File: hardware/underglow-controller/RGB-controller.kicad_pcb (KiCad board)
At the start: 4 copper layers, 86 x 97.7 mm, 139 parts, among them J2 U.FL-R-SMT-1(10), J3 DM3AT-SF-PEJM5, J4 DTM1312PA12PBR008, J5 Conn_01x10, J6 CONSOLE, J7 U.FL-R-SMT-1(10), J8 JTAG, Q2 STS8DNF3LL, Q3 STS8DNF3LL, Q4 STS8DNF3LL, SW2 SW_Push, SW3 SW_Push, SW4 SW_Push, U10 DRV8844PWP, U11 RP2040, U3 SN65HVD230, U4 ESP32-S3R2, U5 W25Q128JVS, U6 WS2815B, U7 W25Q128JVS, U8 ADP2303ARDZ-3.3, U9 COM-13909, Y2 40MHZ, Y3 32.7k, Y4 40MHZ

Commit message: Fill out BOM for mouser
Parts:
- removed C2: 1uF, Capacitor_SMD:C_0402_1005Metric
- removed R2: 442k, Resistor_SMD:R_0402_1005Metric
- AE2: value Antenna_Shield -> PCB_ANT
- AE3: value Antenna_Shield -> PCB_ANT_RFM69
- D5: footprint Diode_SMD:D_SOD-123 -> Diode_SMD:D_SOD-123F
- R23: value 100k -> 10k
- R39: footprint Resistor_SMD:R_0603_1608Metric -> Resistor_SMD:R_0402_1005Metric
- moved D5 0.28 mm to (89.6, 55.2)
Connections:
- U4 pad 36: /SPICLK_N -> unconnected-(U4-Pad36)
- U4 pad 37: /SPICLK_P -> unconnected-(U4-Pad37)
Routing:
- net /SPICLK_P: track 7.04 -> 0.00 mm
- net GND: track 132.8 -> 130.2 mm, vias 79 -> 78
- net Net-(C42-Pad1): track 1.58 -> 2.18 mm

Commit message: gerbertiem
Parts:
- moved C14 0.46 mm to (49.7, 111.3)
- moved C16 0.46 mm to (48.7, 111.3)
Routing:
- net /GPIO_GPO4: track 40.6 -> 38.2 mm
- net /GPIO_GPO1: track 45.3 -> 43.6 mm
- net +3V3: track 535.4 -> 536.3 mm
- net /FSPICLK: track 217.0 -> 217.8 mm
- net /FSPID: track 225.5 -> 226.3 mm
- net /FSPIQ: track 225.8 -> 226.4 mm

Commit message: bom bom bom bom
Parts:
- moved C40 0.11 mm to (46.6, 72.1)
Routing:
- net /SPICS1: track 36.9 -> 0.00 mm, vias 1 -> 0
- net +3V3: track 536.3 -> 528.7 mm, vias 24 -> 32
- net /GPIO_GPO5: track 38.3 -> 35.0 mm
- net GND: track 130.2 -> 129.9 mm, vias 78 -> 81
- net /SW: vias 2 -> 4

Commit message: Submit for fab. tagme
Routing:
- net +3V3: track 528.7 -> 534.2 mm
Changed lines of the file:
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@@
   (segment (start 73.98 76.77) (end 73.98 74.79) (width 1) (layer "B.Cu") (net 13))
   (segment (start 77.9 75.86) (end 79.07 75.86) (width 1) (layer "B.Cu") (net 13))
-  (segment (start 103.61 117.14) (end 103.61 119.22) (width 1) (layer "B.Cu") (net 13))
+  (segment (start 87.74 116.3) (end 89.02 117.58) (width 1) (layer "B.Cu") (net 13))
   (segment (start 39.64 103.97) (end 41.28 105.61) (width 0.5) (layer "B.Cu") (net 13))
   (segment (start 76.69 75.86) (end 77.9 75.86) (width 1) (layer "B.Cu") (net 13))
   (segment (start 56.09 78.1) (end 54.23 79.96) (width 1) (layer "B.Cu") (net 13))
   (segment (start 46.12 72.97) (end 46.12 67.59666) (width 1) (layer "B.Cu") (net 13))
+  (segment (start 89.56 117.04) (end 89.02 117.58) (width 1) (layer "B.Cu") (net 13))
   (segment (start 38.44 125.205) (end 38.44 129.06) (width 0.5) (layer "B.Cu") (net 13))
   (segment (start 55.19 124.81) (end 55.4 124.6) (width 0.5) (layer "B.Cu") (net 13))
   (segment (start 71.18 71.99) (end 71.18 62.33) (width 1) (layer "B.Cu") (net 13))
+  (segment (start 83.23 116.3) (end 87.74 116.3) (width 1) (layer "B.Cu") (net 13))
   (segment (start 55.86 115.92) (end 55.4 116.38) (width 0.5) (layer "B.Cu") (net 13))
-  (segment (start 103.56 117.04) (end 92.35 117.04) (width 1) (layer "B.Cu") (net 13))
   (segment (start 35.06 72.77) (end 35.05 72.78) (width 0.5) (layer "B.Cu") (net 13))
   (segment (start 54.23 79.96) (end 49.7 79.96) (width 1) (layer "B.Cu") (net 13))
@@
   (segment (start 36.81 100.6305) (end 36.81 103.95) (width 0.5) (layer "B.Cu") (net 13))
   (segment (start 55.86 115.92) (end 55.528415 115.588415) (width 1) (layer "B.Cu") (net 13))
-  (segment (start 90.457499 118.932501) (end 90.377499 118.932501) (width 1) (layer "B.Cu") (net 13))
-  (segment (start 103.61 119.22) (end 101.47 121.36) (width 1) (layer "B.Cu") (net 13))
   (segment (start 46.1 67.57666) (end 46.1 65.4) (width 1) (layer "B.Cu") (net 13))
   (segment (start 56.24 116.3) (end 55.86 115.92) (width 1) (layer "B.Cu") (net 13))
@@
   (segment (start 91.14 119.695003) (end 90.377499 118.932501) (width 1) (layer "B.Cu") (net 13))
   (segment (start 41.27 110.27) (end 41.28 110.28) (width 0.5) (layer "B.Cu") (net 13))
+  (segment (start 97.64 119.22) (end 99.78 121.36) (width 1) (layer "B.Cu") (net 13))
   (segment (start 46.1 65.4) (end 42.18 61.48) (width 1) (layer "B.Cu") (net 13))
   (segment (start 53.43 124.81) (end 52.07 123.45) (width 0.5) (layer "B.Cu") (net 13))
@@
   (segment (start 89.024998 117.58) (end 90.377499 118.932501) (width 1) (layer "B.Cu") (net 13))
   (segment (start 35.06 65.27) (end 38.85 61.48) (width 0.5) (layer "B.Cu") (net 13))
-  (segment (start 101.47 121.36) (end 99.78 121.36) (width 1) (layer "B.Cu") (net 13))
   (segment (start 35.51 103.97) (end 36.79 103.97) (width 0.5) (layer "B.Cu") (net 13))
   (segment (start 104.45 79.3) (end 104.43 79.32) (width 1) (layer "B.Cu") (net 13))
@@
   (segment (start 55.528415 115.518415) (end 55.528415 115.588415) (width 0.5) (layer "B.Cu") (net 13))
   (segment (start 35.05 72.78) (end 35.05 75.16) (width 0.5) (layer "B.Cu") (net 13))
-  (segment (start 92.35 117.04) (end 90.457499 118.932501) (width 1) (layer "B.Cu") (net 13))
   (segment (start 43.16 120.485) (end 38.44 125.205) (width 0.5) (layer "B.Cu") (net 13))
+  (segment (start 103.56 117.04) (end 89.56 117.04) (width 1) (layer "B.Cu") (net 13))
   (segment (start 35.05 75.16) (end 37.318816 77.428816) (width 0.5) (layer "B.Cu") (net 13))
   (segment (start 49.7 79.96) (end 46.119992 76.379992) (width 1) (layer "B.Cu") (net 13))
@@
   (segment (start 64.565 55.715) (end 52.39 55.715) (width 1) (layer "B.Cu") (net 13))
   (segment (start 54.893589 114.883589) (end 55.528415 115.518415) (width 0.5) (layer "B.Cu") (net 13))
+  (segment (start 97.64 117.09) (end 97.64 119.22) (width 1) (layer "B.Cu") (net 13))
   (segment (start 52.786828 112.78) (end 49.18 112.78) (width 0.5) (layer "B.Cu") (net 13))
   (segment (start 54.890417 114.883589) (end 52.786828 112.78) (width 0.5) (layer "B.Cu") (net 13))

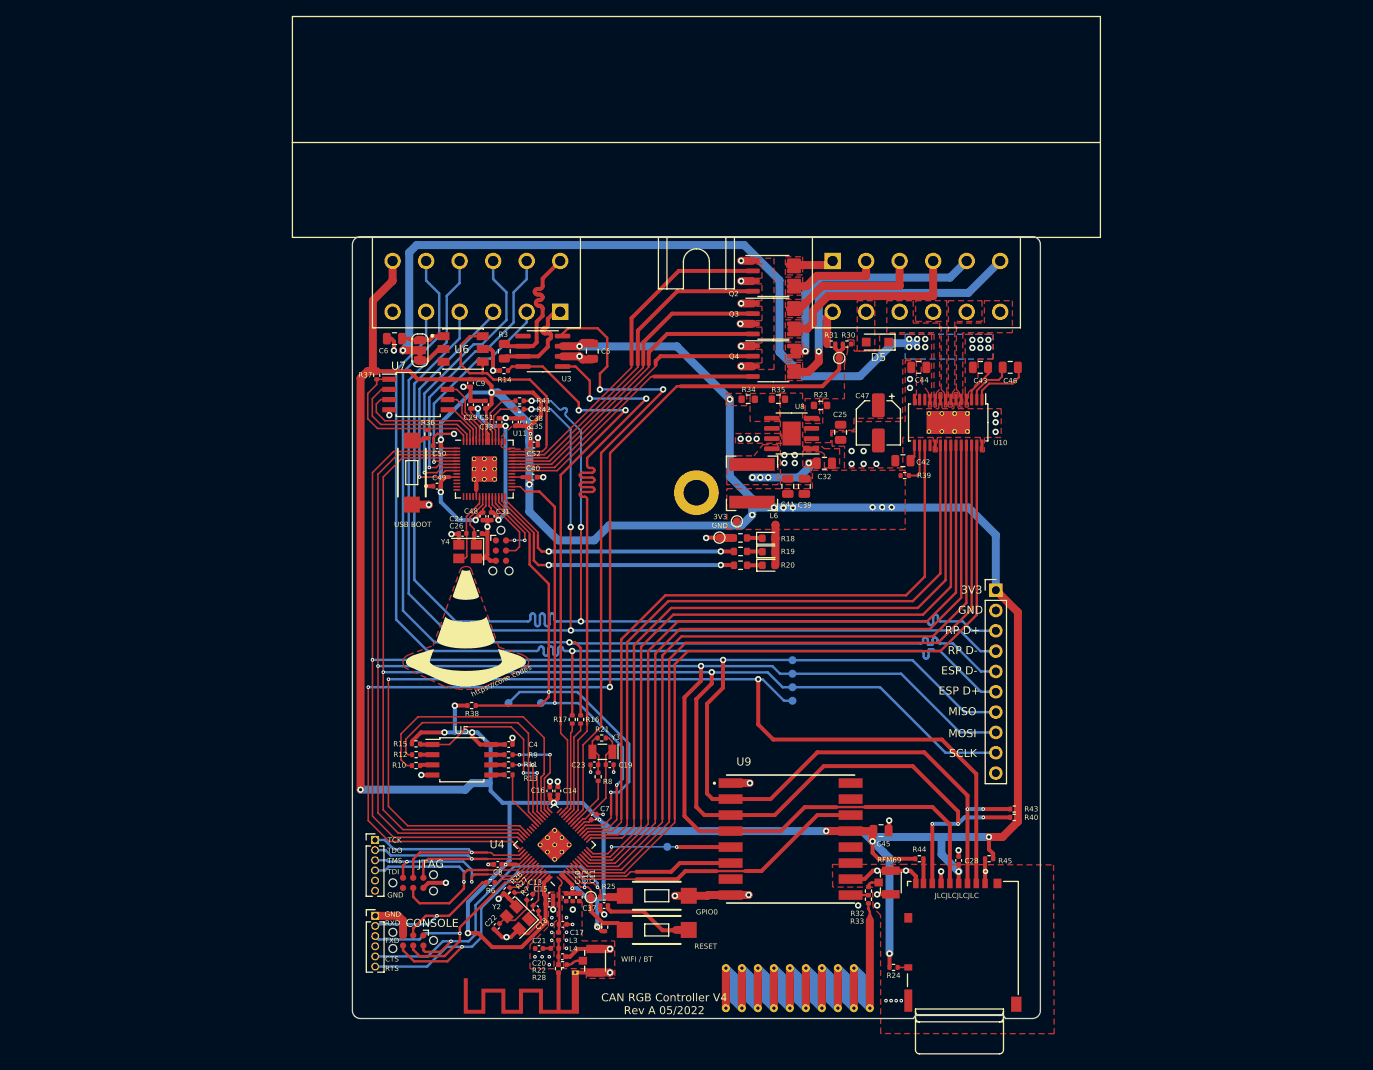
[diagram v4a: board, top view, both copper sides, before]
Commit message: hardware updates: fix SPI bus on pico and flatten radio module
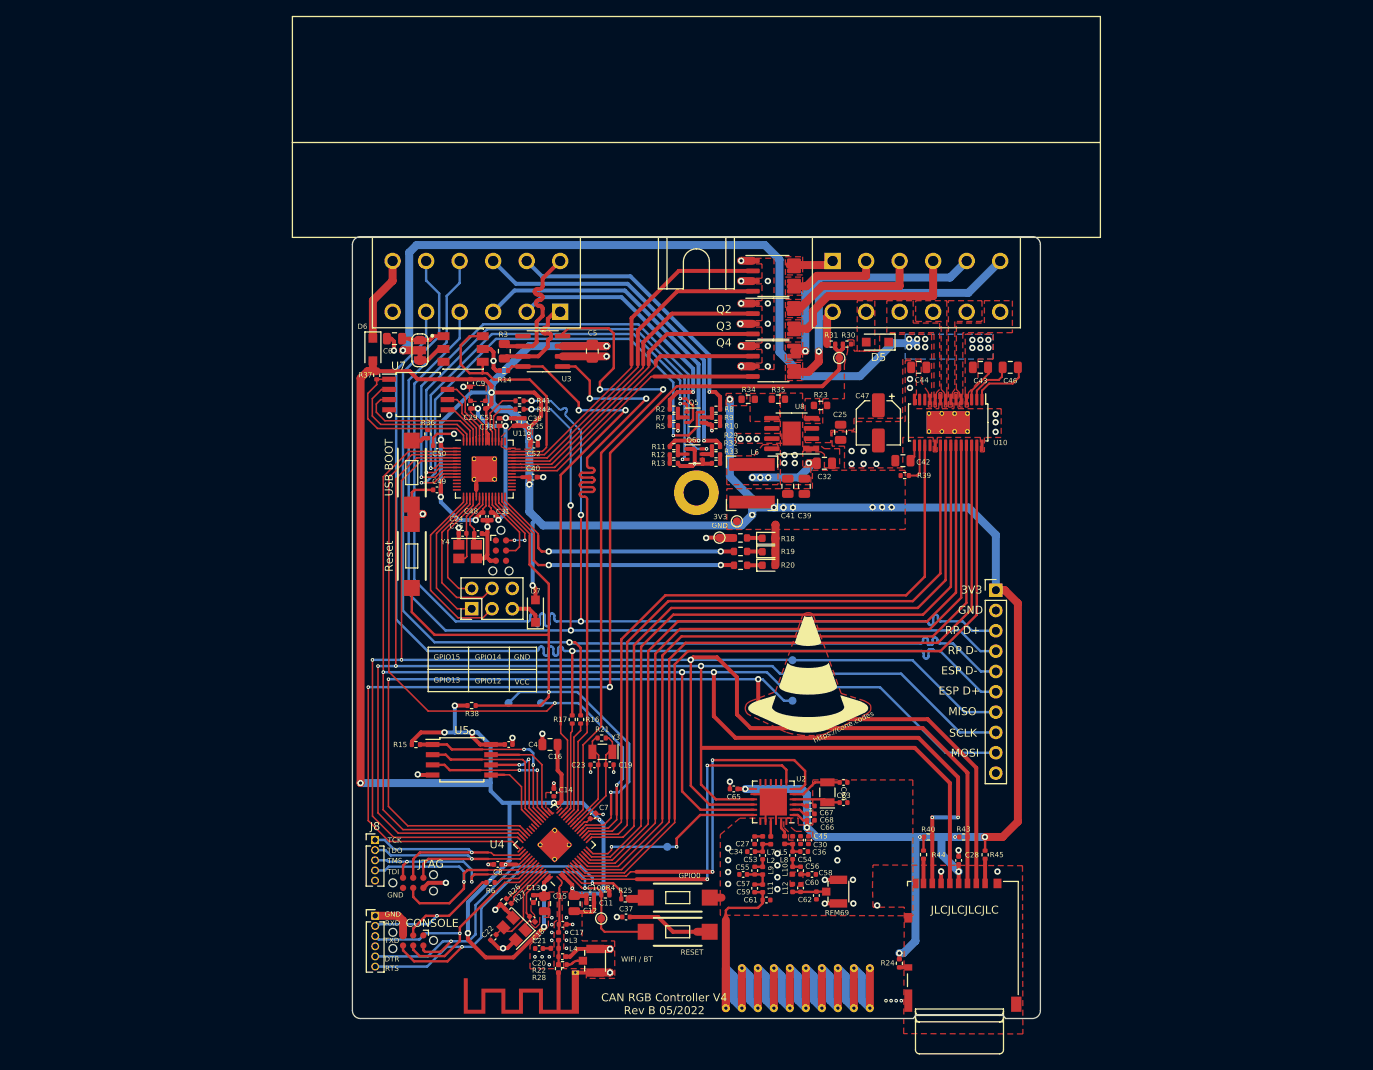
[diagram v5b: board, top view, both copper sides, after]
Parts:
- removed U9: COM-13909, ConeCodes:XCVR_RFM69HW
- added C27: C_Small, Capacitor_SMD:C_0402_1005Metric, F.Cu at (74.3, 117.5)
- added C30: C_Small, Capacitor_SMD:C_0402_1005Metric, F.Cu at (80.0, 117.4)
- added C34: C_Small, Capacitor_SMD:C_0402_1005Metric, F.Cu at (73.8, 118.9)
- added C36: C_Small, Capacitor_SMD:C_0402_1005Metric, F.Cu at (80.5, 118.9)
- added C53: C_Small, Capacitor_SMD:C_0402_1005Metric, F.Cu at (75.3, 119.3)
- added C54: C_Small, Capacitor_SMD:C_0402_1005Metric, F.Cu at (79.0, 119.3)
- added C55: C_Small, Capacitor_SMD:C_0402_1005Metric, F.Cu at (74.3, 121.2)
- added C56: C_Small, Capacitor_SMD:C_0402_1005Metric, F.Cu at (80.0, 121.2)
- added C57: C_Small, Capacitor_SMD:C_0402_1005Metric, F.Cu at (72.8, 121.7)
- added C58: C_Small, Capacitor_SMD:C_0402_1005Metric, F.Cu at (81.5, 121.7)
- added C59: C_Small, Capacitor_SMD:C_0402_1005Metric, F.Cu at (74.3, 123.5)
- added C60: C_Small, Capacitor_SMD:C_0402_1005Metric, F.Cu at (80.0, 123.4)
- added C61: C_Small, Capacitor_SMD:C_0402_1005Metric, F.Cu at (75.8, 124.9)
- added C62: C_Small, Capacitor_SMD:C_0402_1005Metric, F.Cu at (82.0, 124.3)
- added C63: 10pF, Capacitor_SMD:C_0402_1005Metric, F.Cu at (85.4, 112.7)
- added C64: 10pF, Capacitor_SMD:C_0402_1005Metric, F.Cu at (85.4, 110.2)
- added C65: 0.1uF, Capacitor_SMD:C_0402_1005Metric, F.Cu at (71.7, 111.0)
- added C66: 0.1uF, Capacitor_SMD:C_0402_1005Metric, F.Cu at (81.3, 115.0)
- added C67: 0.1uF, Capacitor_SMD:C_0402_1005Metric, F.Cu at (81.3, 113.2)
- added C68: 0.1uF, Capacitor_SMD:C_0402_1005Metric, F.Cu at (81.3, 114.2)
- added D6: D_Small, Diode_SMD:D_SOD-123F, F.Cu at (26.6, 56.1)
- added D7: D_Small, Diode_SMD:D_SOD-123F, F.Cu at (46.9, 88.8)
- added J9: Conn_01x10, Connector_PinHeader_2.54mm:PinHeader_2x03_P2.54mm_Vertical, F.Cu at (38.9, 88.5)
- added L10: L_Small, Inductor_SMD:L_0402_1005Metric, F.Cu at (79.0, 121.2)
- added L11: L_Small, Inductor_SMD:L_0402_1005Metric, F.Cu at (75.3, 123.5)
- added L12: L_Small, Inductor_SMD:L_0402_1005Metric, F.Cu at (79.0, 123.4)
- added L2: L_Small, Inductor_SMD:L_0402_1005Metric, F.Cu at (76.3, 117.5)
- added L5: L_Small, Inductor_SMD:L_0402_1005Metric, F.Cu at (78.0, 117.4)
- added L7: L_Small, Inductor_SMD:L_0402_1005Metric, F.Cu at (75.3, 117.5)
- added L8: L_Small, Inductor_SMD:L_0402_1005Metric, F.Cu at (79.0, 117.4)
- added L9: L_Small, Inductor_SMD:L_0402_1005Metric, F.Cu at (75.3, 121.2)
- added Q5: MBT3904DW1T1G, Package_TO_SOT_SMD:SOT-363_SC-70-6, F.Cu at (66.8, 64.6)
- added Q6: MBT3904DW1T1G, Package_TO_SOT_SMD:SOT-363_SC-70-6, F.Cu at (66.8, 69.2)
- added R2: 10k, Resistor_SMD:R_0402_1005Metric, F.Cu at (64.2, 63.6)
- added R29: 10k, Resistor_SMD:R_0402_1005Metric, F.Cu at (69.5, 68.2)
- added R5: 1k, Resistor_SMD:R_0402_1005Metric, F.Cu at (64.2, 64.6)
- added SW5: SW_Push, ConeCodes:SW_RS-032G05A3-SMRT, F.Cu at (31.4, 81.9)
- added U2: SX1231HIMLTRT, Package_DFN_QFN:QFN-24-1EP_5x5mm_P0.65mm_EP3.4x3.4mm, F.Cu at (76.6, 112.7)
- added Y5: 32.7k, Crystal:Crystal_SMD_MicroCrystal_CC7V-T1A-2Pin_3.2x1.5mm, F.Cu at (83.4, 111.5)
- C12, C15: footprint Capacitor_SMD:C_0402_1005Metric -> Capacitor_SMD:C_0805_2012Metric
- C16: value 1uF -> 10uF; footprint Capacitor_SMD:C_0402_1005Metric -> Capacitor_SMD:C_0805_2012Metric
- C45: value 10uF -> C_Small; footprint Capacitor_SMD:C_0805_2012Metric -> Capacitor_SMD:C_0402_1005Metric
- J8: footprint Connector_PinHeader_1.27mm:PinHeader_1x06_P1.27mm_Vertical -> Connector_PinHeader_1.27mm:PinHeader_1x05_P1.27mm_Vertical
- L6: value 6.8uh -> 4.7uH
- R10, R13, R33, R7: value 0R -> 499R
- R11, R8: value 0R -> 10k
- R12, R32, R9: value 0R -> 1k
- Y4: value 40MHZ -> 12MHZ
- moved R7 61.6 mm to (64.2, 65.6), turned to 0 degrees
- moved R32 57.8 mm to (69.5, 69.3), turned to 0 degrees
- moved R33 57.7 mm to (69.5, 70.3), turned to 180 degrees
- moved R10 56.7 mm to (69.5, 65.6)
- moved R9 49.5 mm to (69.5, 64.6)
- moved R12 49.4 mm to (64.2, 69.3)
- moved R8 48.2 mm to (69.5, 63.6), turned to 180 degrees
- moved R11 44.8 mm to (64.2, 68.2)
- moved R13 44.1 mm to (64.2, 70.3)
- moved G*** 43.2 mm to (81.0, 96.7)
- moved R40 11.0 mm to (96.0, 117.0), turned to 0 degrees
- moved C45 9.14 mm to (81.0, 117.4), turned to -90 degrees
- moved R43 7.25 mm to (100.4, 117.0), turned to 0 degrees
- moved J2 6.65 mm to (84.8, 123.9)
- moved C16 5.80 mm to (48.7, 105.5), turned to 180 degrees
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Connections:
- C45 pad 1: GND -> /VR_PA
- C45 pad 2: +3V3 -> GND
- J4 pad B10: /CONN_B10 -> /GPI3
- J4 pad B11: /CONN_B11 -> /GPI1
- J4 pad B2: /CONN_B2 -> /GPI2
- J4 pad B3: /CONN_B3 -> /GPI4
- J4 pad B7: +3V3 -> /V33OUT
- R10 pad 1: /SPIWP -> Net-(R10-Pad1)
- R10 pad 2: Net-(R10-Pad2) -> GND
- R11 pad 1: /SPICLK -> /GPI4
- R11 pad 2: Net-(R11-Pad2) -> Net-(Q6-Pad2)
- R12 pad 1: /SPIQ -> Net-(Q6-Pad2)
- R13 pad 1: /SPID -> Net-(R12-Pad2)
- R13 pad 2: Net-(R13-Pad2) -> GND
- R32 pad 1: /RF69_RF_ANT -> Net-(Q6-Pad5)
- R32 pad 2: /RF69_RF_EXT -> Net-(R32-Pad2)
- R33 pad 1: /RF69_RF_ANT -> Net-(R32-Pad2)
- R33 pad 2: /RF69_RF_ANT_PCB -> GND
- R7 pad 1: /XTAL_N -> Net-(R5-Pad2)
- R7 pad 2: Net-(R7-Pad2) -> GND
- R8 pad 1: /RTC_XTAL_N -> /GPI1
- R8 pad 2: Net-(R8-Pad2) -> Net-(Q5-Pad5)
- R9 pad 1: /SPIHD -> Net-(Q5-Pad5)
- R9 pad 2: Net-(R9-Pad2) -> Net-(R10-Pad1)
- U11 pad 15: unconnected-(U11-Pad15) -> /RP_GPIO12
- U11 pad 16: unconnected-(U11-Pad16) -> /RP_GPIO13
- U11 pad 17: unconnected-(U11-Pad17) -> /RP_GPIO14
- U11 pad 18: unconnected-(U11-Pad18) -> /RP_GPIO15
- U11 pad 2: /FSPIQ -> /FSPID
- U11 pad 3: /FSPICLK -> /FSPICS2
- U11 pad 30: /FSPICS2 -> unconnected-(U11-Pad30)
- U11 pad 4: /FSPID -> /FSPICLK
- U11 pad 5: /CONN_B2 -> /FSPIQ
- U11 pad 6: /CONN_B11 -> /GPIO_GPI1
- U11 pad 7: /CONN_B10 -> /GPIO_GPI3
- U11 pad 8: /CONN_B3 -> /GPIO_GPI4
- U11 pad 9: unconnected-(U11-Pad9) -> /GPIO_GPI2
- U4 pad 22: Net-(R8-Pad2) -> /RTC_XTAL_N
- U4 pad 30: Net-(R9-Pad2) -> /SPIHD
- U4 pad 31: Net-(R10-Pad2) -> /SPIWP
- U4 pad 33: Net-(R11-Pad2) -> /SPICLK
- U4 pad 34: Net-(R12-Pad2) -> /SPIQ
- U4 pad 35: Net-(R13-Pad2) -> /SPID
- U4 pad 38: /FSPIHD -> unconnected-(U4-Pad38)
- U4 pad 53: Net-(R7-Pad2) -> /XTAL_N
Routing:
- net /GPIO_GPI4: track 0.00 -> 66.9 mm, vias 0 -> 2
- net /GPIO_GPI2: track 0.00 -> 64.0 mm, vias 0 -> 2
- net /GPIO_GPI3: track 0.00 -> 63.2 mm, vias 0 -> 2
- net /GPIO_GPI1: track 0.00 -> 56.2 mm, vias 0 -> 2
- net /GPI4: track 0.00 -> 44.1 mm, vias 0 -> 1
- net /GPI3: track 0.00 -> 44.0 mm, vias 0 -> 1
- net /CONN_B10: track 36.3 -> 0.00 mm, vias 1 -> 0
- net /GPI1: track 0.00 -> 35.4 mm, vias 0 -> 1
- net /CONN_B11: track 35.2 -> 0.00 mm, vias 1 -> 0
- net Net-(R10-Pad2): track 34.8 -> 0.00 mm
- net /GPI2: track 0.00 -> 32.7 mm, vias 0 -> 1
- net Net-(R12-Pad2): track 30.9 -> 1.07 mm
- net /CONN_B3: track 29.0 -> 0.00 mm, vias 1 -> 0
- net /CONN_B2: track 27.3 -> 0.00 mm, vias 1 -> 0
- net /GPIO2: track 21.1 -> 47.9 mm, vias 0 -> 2
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- added copper zone on F.Cu, net /VR_PA
- added copper zone on F.Cu, net Net-(C56-Pad2)
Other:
- board text added: "CAN RGB Controller V4 Rev B 05/2022"
- board text added: "DTR"
- board text added: "GPIO12"
- board text added: "GPIO13"
- board text added: "GPIO14"
- board text added: "GPIO15"
- board text added: "Reset"
- board text added: "VCC"
- board text removed: "CAN RGB Controller V4 Rev A 05/2022"
- board text removed: "CTS"
